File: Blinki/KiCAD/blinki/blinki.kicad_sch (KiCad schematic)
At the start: 10 parts, among them Q1 Q_NPN_CBE, Q2 Q_NPN_CBE

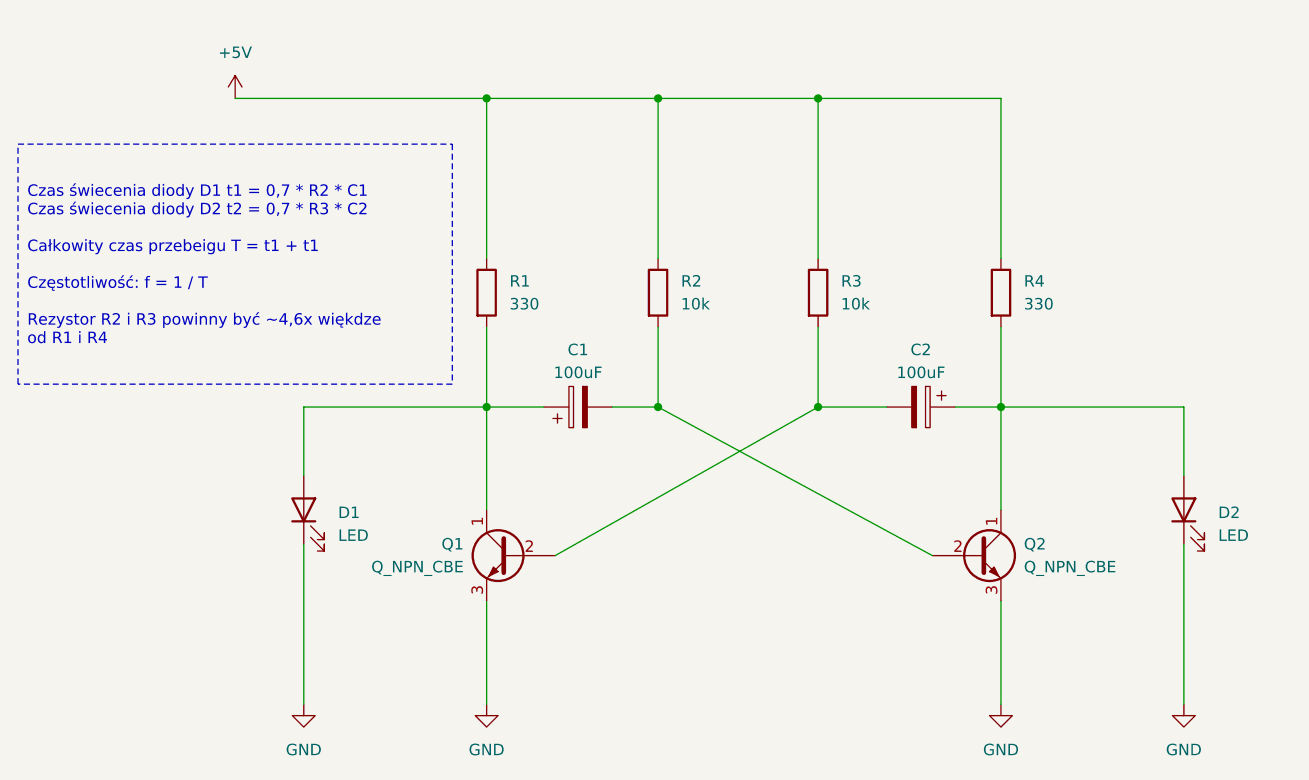
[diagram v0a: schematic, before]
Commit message: Fixes ERC errors by adding power flags.
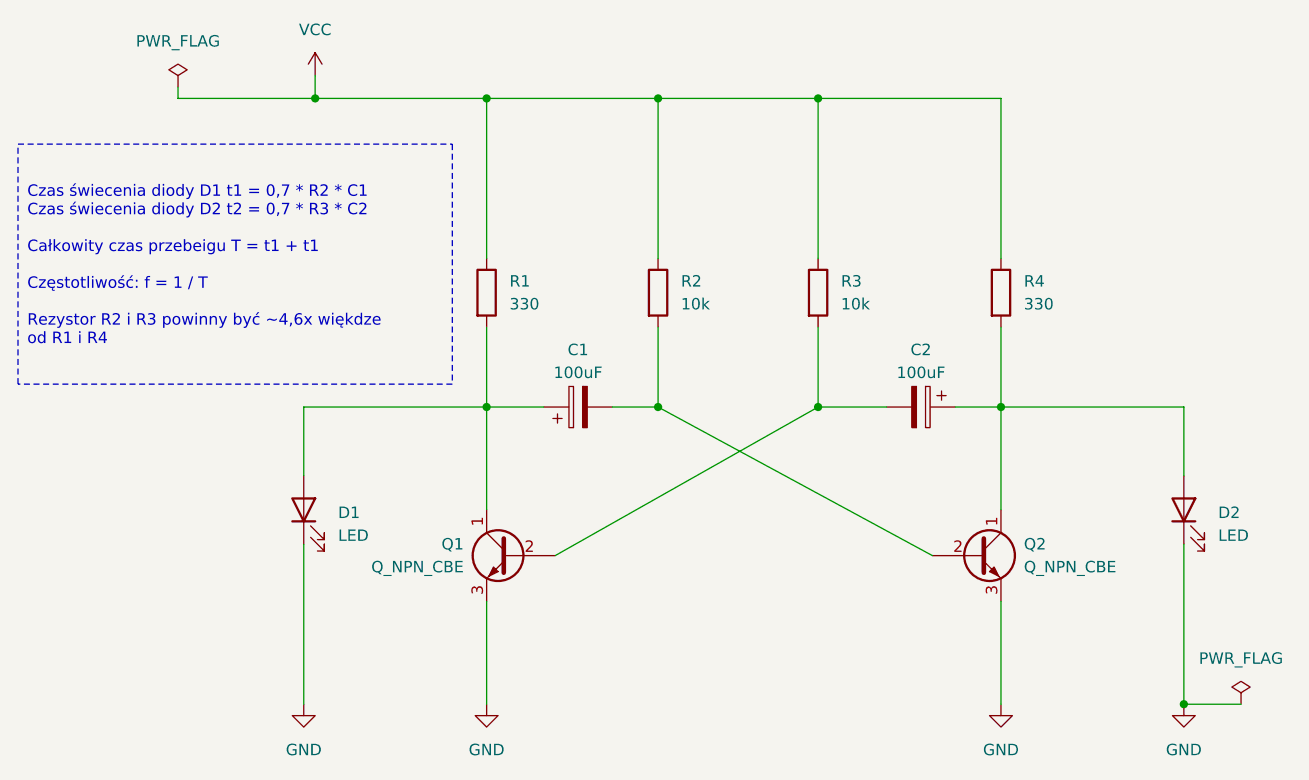
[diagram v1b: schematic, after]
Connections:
- net +5V renamed VCC
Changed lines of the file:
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@@
   (junction (at 116.84 53.34) (diameter 0) (color 0 0 0 0)
   )
+  (junction (at 194.31 120.65) (diameter 0) (color 0 0 0 0)
+  )
   (junction (at 135.89 87.63) (diameter 0) (color 0 0 0 0)
   )
   (junction (at 153.67 87.63) (diameter 0) (color 0 0 0 0)
   )
+  (junction (at 97.79 53.34) (diameter 0) (color 0 0 0 0)
+  )
   (junction (at 173.99 87.63) (diameter 0) (color 0 0 0 0)
   )
+  (wire (pts (xy 82.55 53.34) (xy 97.79 53.34))
+    (stroke (width 0) (type default))
+  )
   (wire (pts (xy 173.99 87.63) (xy 194.31 87.63))
     (stroke (width 0) (type default))
@@
     (stroke (width 0) (type default))
   )
+  (wire (pts (xy 200.66 120.65) (xy 194.31 120.65))
+    (stroke (width 0) (type default))
+  )
   (wire (pts (xy 194.31 102.87) (xy 194.31 120.65))
     (stroke (width 0) (type default))
@@
     (stroke (width 0) (type default))
   )
+  (wire (pts (xy 97.79 50.8) (xy 97.79 53.34))
+    (stroke (width 0) (type default))
+  )
   (wire (pts (xy 116.84 87.63) (xy 96.52 87.63))
     (stroke (width 0) (type default))
@@
     (stroke (width 0) (type default))
   )
-  (wire (pts (xy 116.84 53.34) (xy 88.9 53.34))
+  (wire (pts (xy 116.84 53.34) (xy 97.79 53.34))
     (stroke (width 0) (type default))
   )
@@
   )
   (wire (pts (xy 135.89 87.63) (xy 130.81 87.63))
+    (stroke (width 0) (type default))
+  )
+  (wire (pts (xy 82.55 52.07) (xy 82.55 53.34))
     (stroke (width 0) (type default))
   )
@@
     )
   )
-  (symbol (lib_id "power:+5V") (at 88.9 53.34 0) (unit 1)
-    (in_bom yes) (on_board yes) (dnp no) (fields_autoplaced)
-    (property "Reference" "#PWR01" (at 88.9 57.15 0)
-      (effects (font (size 1.27 1.27)) hide)
-    )
-    (property "Value" "+5V" (at 88.9 48.26 0)
-      (effects (font (size 1.27 1.27)))
-    )
-    (property "Footprint" "" (at 88.9 53.34 0)
-      (effects (font (size 1.27 1.27)) hide)
-    )
-    (property "Datasheet" "" (at 88.9 53.34 0)
-      (effects (font (size 1.27 1.27)) hide)
-    )
-    (pin "1")
-    (instances
-      (project "blinki"
-        (path "/4c6f2aa9-5248-476e-a7ca-a4e69d074d06"
-          (reference "#PWR01") (unit 1)
-        )
-      )
-    )
-  )
   (symbol (lib_id "power:GND") (at 173.99 120.65 0) (unit 1)
     (in_bom yes) (on_board yes) (dnp no) (fields_autoplaced)
@@
         (path "/4c6f2aa9-5248-476e-a7ca-a4e69d074d06"
           (reference "R4") (unit 1)
+        )
+      )
+    )
+  )
+  (symbol (lib_id "power:PWR_FLAG") (at 82.55 52.07 0) (unit 1)
+    (in_bom yes) (on_board yes) (dnp no) (fields_autoplaced)
+    (property "Reference" "#FLG01" (at 82.55 50.165 0)
+      (effects (font (size 1.27 1.27)) hide)
+    )
+    (property "Value" "PWR_FLAG" (at 82.55 46.99 0)
+      (effects (font (size 1.27 1.27)))
+    )
+    (property "Footprint" "" (at 82.55 52.07 0)
+      (effects (font (size 1.27 1.27)) hide)
+    )
+    (property "Datasheet" "~" (at 82.55 52.07 0)
+      (effects (font (size 1.27 1.27)) hide)
+    )
+    (pin "1")
+    (instances
+      (project "blinki"
+        (path "/4c6f2aa9-5248-476e-a7ca-a4e69d074d06"
+          (reference "#FLG01") (unit 1)
         )
       )
@@
     )
   )
+  (symbol (lib_id "power:VCC") (at 97.79 50.8 0) (unit 1)
+    (in_bom yes) (on_board yes) (dnp no) (fields_autoplaced)
+    (property "Reference" "#PWR01" (at 97.79 54.61 0)
+      (effects (font (size 1.27 1.27)) hide)
+    )
+    (property "Value" "VCC" (at 97.79 45.72 0)
+      (effects (font (size 1.27 1.27)))
+    )
+    (property "Footprint" "" (at 97.79 50.8 0)
+      (effects (font (size 1.27 1.27)) hide)
+    )
+    (property "Datasheet" "" (at 97.79 50.8 0)
+      (effects (font (size 1.27 1.27)) hide)
+    )
+    (pin "1")
+    (instances
+      (project "blinki"
+        (path "/4c6f2aa9-5248-476e-a7ca-a4e69d074d06"
+          (reference "#PWR01") (unit 1)
+        )
+      )
+    )
+  )
   (symbol (lib_id "Device:LED") (at 96.52 99.06 90) (unit 1)
     (in_bom yes) (on_board yes) (dnp no) (fields_autoplaced)
@@
         )
       )
+    )
+  )
+  (symbol (lib_id "power:PWR_FLAG") (at 200.66 120.65 0) (unit 1)
+    (in_bom yes) (on_board yes) (dnp no) (fields_autoplaced)
+    (property "Reference" "#FLG02" (at 200.66 118.745 0)
+      (effects (font (size 1.27 1.27)) hide)
+    )
+    (property "Value" "PWR_FLAG" (at 200.66 115.57 0)
+      (effects (font (size 1.27 1.27)))
+    )
+    (property "Footprint" "" (at 200.66 120.65 0)
+      (effects (font (size 1.27 1.27)) hide)
+    )
+    (property "Datasheet" "~" (at 200.66 120.65 0)
+      (effects (font (size 1.27 1.27)) hide)
+    )
+    (pin "1")
+    (instances
+      (project "blinki"
+        (path "/4c6f2aa9-5248-476e-a7ca-a4e69d074d06"
+          (reference "#FLG02") (unit 1)
+        )
+      )
